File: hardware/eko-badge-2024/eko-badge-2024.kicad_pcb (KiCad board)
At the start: 2 copper layers, 45 x 95 mm, 1 part

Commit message: feat(Hw):Added_Lentes_project
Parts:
- removed the Ref** at (128.2, 66.4)
- added REF**: PinSocket_2x03_P2.54mm_Vertical, Connector_PinSocket_2.54mm:PinSocket_2x03_P2.54mm_Vertical, F.Cu at (190.4, 70.9)
- added Ref**: Val**, Eko2024:llama 1 flaca, F.Cu at (203.5, 80.0)
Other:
- board size 45 x 95 mm -> 47.5 x 99.9 mm

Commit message: feat(Hw):Added_First_Route
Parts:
- removed REF**: PinSocket_2x03_P2.54mm_Vertical, Connector_PinSocket_2.54mm:PinSocket_2x03_P2.54mm_Vertical
- added AE1: Antenna_Shield, Eko2024:SMA_EDGE, B.Cu at (221.3, 109.9)
- added C1: 10uF, Capacitor_SMD:C_0603_1608Metric, B.Cu at (221.5, 47.7)
- added C10: .1uF, Capacitor_SMD:C_0603_1608Metric, F.Cu at (194.1, 126.0)
- added C11: .1uF, Capacitor_SMD:C_0603_1608Metric, F.Cu at (205.4, 118.5)
- added C12: 0.1uF, Capacitor_SMD:C_0603_1608Metric, B.Cu at (204.2, 112.5)
- added C13: .22uF, Capacitor_SMD:C_0603_1608Metric, B.Cu at (202.1, 107.5)
- added C14: .1uF, Capacitor_SMD:C_0603_1608Metric, B.Cu at (211.2, 107.5)
- added C15: 1uF, Capacitor_SMD:C_0603_1608Metric, B.Cu at (207.2, 112.5)
- added C16: 0.1uF, Capacitor_SMD:C_0603_1608Metric, F.Cu at (207.7, 107.9)
- added C17: 0.1uF, Capacitor_SMD:C_0603_1608Metric, F.Cu at (194.6, 69.3)
- added C18: 0.1uF, Capacitor_SMD:C_0603_1608Metric, F.Cu at (216.1, 69.1)
- added C2: 1uF, Capacitor_SMD:C_0603_1608Metric, B.Cu at (189.6, 106.7)
- added C3: 10uF, Capacitor_SMD:C_0603_1608Metric, B.Cu at (219.3, 44.0)
- added C4: 10uF, Capacitor_SMD:C_0603_1608Metric, B.Cu at (186.8, 106.7)
- added C5: 10uF, Capacitor_SMD:C_0603_1608Metric, B.Cu at (186.7, 108.3)
- added C6: .1uF, Capacitor_SMD:C_0603_1608Metric, F.Cu at (201.9, 120.9)
- added C7: .1uF, Capacitor_SMD:C_0603_1608Metric, F.Cu at (202.6, 117.5)
- added C8: .1uF, Capacitor_SMD:C_0603_1608Metric, F.Cu at (204.6, 121.5)
- added C9: .1uF, Capacitor_SMD:C_0603_1608Metric, F.Cu at (210.7, 124.4)
- added D1: MBR120, Diode_SMD:D_SOD-123F, B.Cu at (221.4, 41.1)
- added D2: WS2812B, LED_SMD:LED_WS2812B-Mini_PLCC4_3.5x3.5mm, F.Cu at (203.6, 107.5)
- added D3: WS2812B, LED_SMD:LED_WS2812B-Mini_PLCC4_3.5x3.5mm, F.Cu at (194.1, 72.1)
- added D4: WS2812B, LED_SMD:LED_WS2812B-Mini_PLCC4_3.5x3.5mm, F.Cu at (217.2, 71.9)
- added F1: 0.75A, Fuse:Fuse_0805_2012Metric, B.Cu at (191.4, 46.8)
- added J1: UART, Connector_PinHeader_2.54mm:PinHeader_1x04_P2.54mm_Vertical, B.Cu at (184.2, 76.0)
- added J2: Battery, Eko2024:BH-AA-A1AJ020, B.Cu at (212.3, 77.6)
- added J3: Lentes, Connector_PinSocket_2.54mm:PinSocket_2x03_P2.54mm_Vertical, F.Cu at (185.0, 68.3)
- added J4: OLED, Eko2024:Display OLED 128 x32, F.Cu at (189.0, 95.6)
- added J7: Battery, Eko2024:BH-AA-A1AJ020, B.Cu at (194.1, 77.6)
- added LS1: 931-SPKM.20.8.A-ND, Connector_PinHeader_1.27mm:PinHeader_1x02_P1.27mm_Vertical, F.Cu at (213.5, 110.9)
- added P1: USB_C_Plug_USB2.0, Eko2024:C393939, B.Cu at (187.5, 43.3)
- added Q1: DMG3415U-7, Package_TO_SOT_SMD:SOT-23, B.Cu at (220.9, 38.0)
- added R1: 100K, Resistor_SMD:R_0603_1608Metric, B.Cu at (224.4, 44.0)
- added R2: 10K, Resistor_SMD:R_0603_1608Metric, B.Cu at (189.6, 108.2)
- added R3: 5k1, Resistor_SMD:R_0603_1608Metric, B.Cu at (191.2, 45.0)
- added R4: 5k1, Resistor_SMD:R_0603_1608Metric, B.Cu at (191.2, 43.5)
- added R5: 47K, Resistor_SMD:R_0603_1608Metric, B.Cu at (200.5, 107.5)
- added R6: 22K, Resistor_SMD:R_0603_1608Metric, B.Cu at (211.2, 110.5)
- added R7: 470, Resistor_SMD:R_0603_1608Metric, B.Cu at (198.0, 107.9)
- added R8: 3.3K, Resistor_SMD:R_0603_1608Metric, B.Cu at (195.7, 107.9)
- added SW1: ON, Eko2024:MSK12C02, B.Cu at (224.2, 79.0)
- added SW2: LEFT, Button_Switch_SMD:SW_SPST_TL3342, F.Cu at (196.9, 119.5)
- added SW3: UP, Button_Switch_SMD:SW_SPST_TL3342, F.Cu at (203.3, 113.7)
- added SW4: DOWN, Button_Switch_SMD:SW_SPST_TL3342, F.Cu at (203.3, 125.4)
- added SW5: RESET, Button_Switch_SMD:SW_SPST_TL3342, F.Cu at (216.5, 126.6)
- added SW6: BOOT, Button_Switch_SMD:SW_SPST_TL3342, F.Cu at (187.8, 126.8)
- added SW7: RIGTH, Button_Switch_SMD:SW_SPST_TL3342, F.Cu at (210.5, 119.5)
- added U1: ESP32-C6-WROOM-1-N4, bsides:XCVR_ESP32-C6-WROOM-1-N8, B.Cu at (189.6, 119.4)
- added U2: AP2112K-3.3, Package_TO_SOT_SMD:SOT-23-5, B.Cu at (221.8, 44.6)
- added U3: RFM95W-868S2, RF_Module:HOPERF_RFM9XW_SMD, B.Cu at (211.9, 121.5)
- added U4: TPA321, Package_SO:SOP-8_3.9x4.9mm_P1.27mm, B.Cu at (206.6, 108.5)
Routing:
- net /VOUT: track 0.00 -> 190.5 mm, vias 0 -> 4
- net /D+: track 0.00 -> 88.8 mm, vias 0 -> 2
- net /D-: track 0.00 -> 86.0 mm, vias 0 -> 2
- net /RX: track 0.00 -> 63.7 mm, vias 0 -> 2
- net /EN: track 0.00 -> 60.0 mm, vias 0 -> 1
- net /TX: track 0.00 -> 59.9 mm, vias 0 -> 2
- net Net-(D2-DOUT): track 0.00 -> 59.2 mm, vias 0 -> 2
- net Net-(D1-K): track 0.00 -> 54.5 mm, vias 0 -> 2
- net GND: track 0.00 -> 50.5 mm, vias 0 -> 7
- net /DIO2: track 0.00 -> 47.8 mm, vias 0 -> 2
- net VBUS: track 0.00 -> 47.4 mm
- net /DIO0: track 0.00 -> 42.2 mm, vias 0 -> 2
- net Net-(D3-DOUT): track 0.00 -> 37.5 mm
- net /DIO1: track 0.00 -> 37.4 mm, vias 0 -> 2
- net /RIGHT: track 0.00 -> 32.6 mm, vias 0 -> 1
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- added copper zone on B.Cu, net GND
- added copper zone on F.Cu, net GND

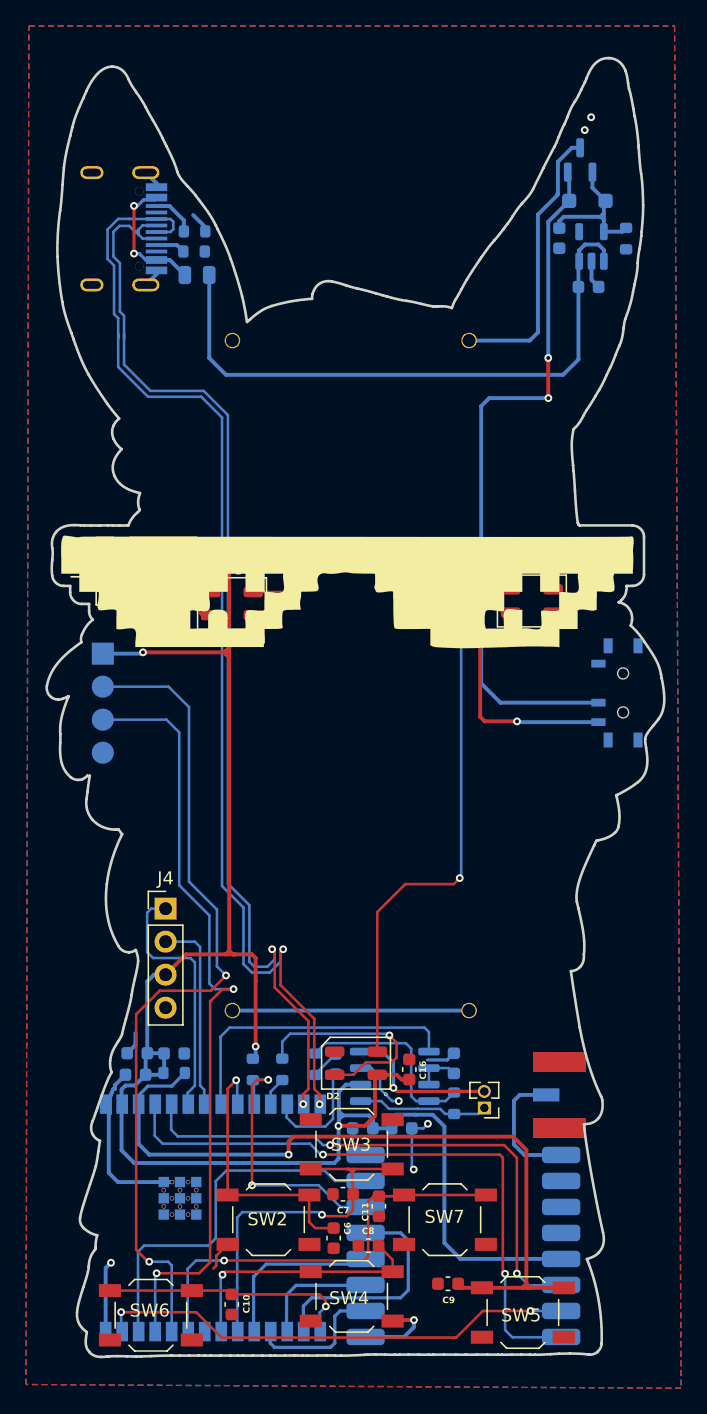
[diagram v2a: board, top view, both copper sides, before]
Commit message: feat(Hw):Update_Layer_Distribution
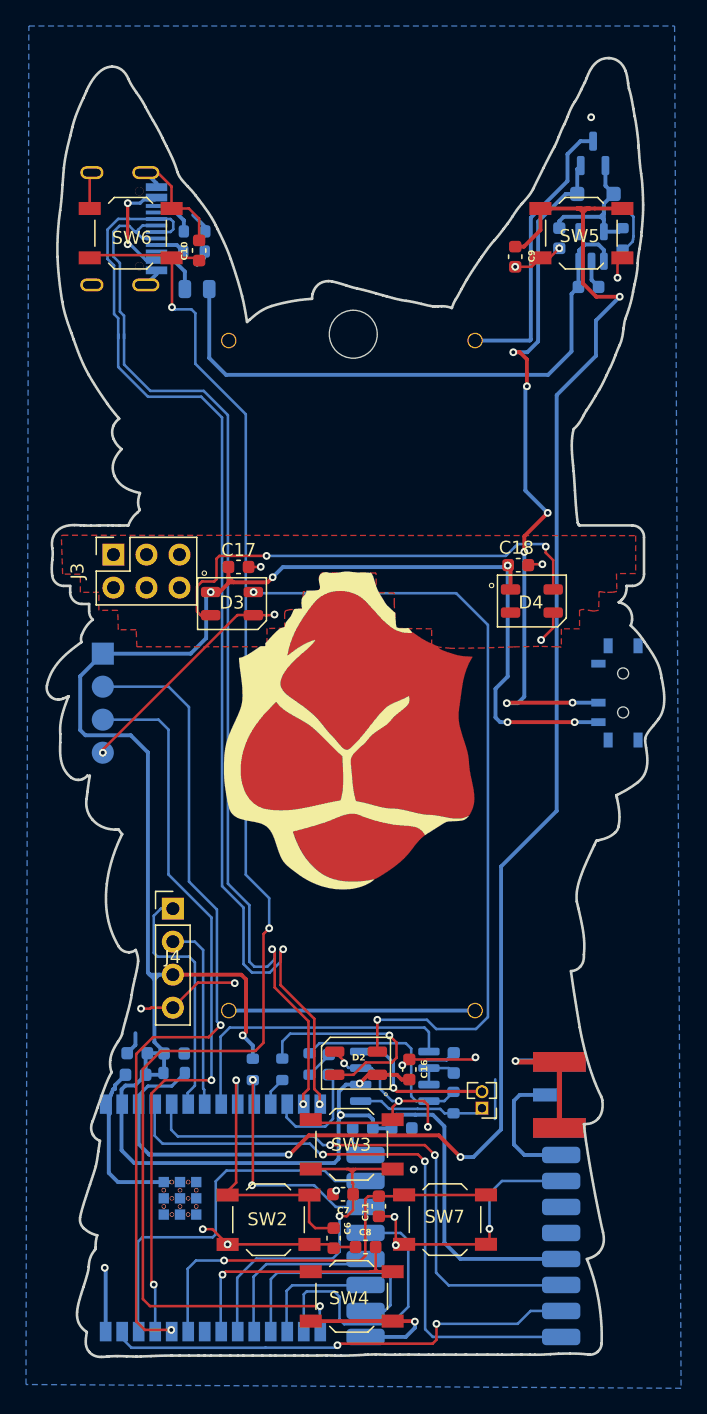
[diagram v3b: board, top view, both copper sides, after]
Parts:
- removed the Ref** at (203.5, 80.0)
- added Ref**: Val**, Eko2024:llama mask flaca, F.Cu at (203.7, 80.0)
- added Ref**: Val**, Eko2024:llama intermedia, F.Cu at (203.7, 80.1)
- moved SW6 83.3 mm to (186.3, 43.6), turned to 0 degrees
- moved SW5 83.2 mm to (221.0, 43.6)
- moved C10 81.1 mm to (191.6, 44.9), turned to -90 degrees
- moved C9 79.2 mm to (215.9, 45.4), turned to 90 degrees
- moved Q1 1.12 mm to (221.9, 37.5)
- moved F1 1.08 mm to (191.4, 47.9)
- moved D1 0.82 mm to (222.1, 40.6)
- moved J4 0.56 mm to (189.5, 95.6)
- moved C13 0.51 mm to (201.5, 107.6)
- moved J2 0.46 mm to (212.8, 77.6)
- moved R5 0.44 mm to (200.1, 107.5)
- moved J7 0.28 mm to (193.8, 77.6)
- moved R1 0.27 mm to (224.1, 44.0)
- moved C8 0.24 mm to (204.4, 121.6)
- moved LS1 0.18 mm to (213.3, 110.9)
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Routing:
- net GND: track 50.5 -> 170.4 mm, vias 7 -> 26
- net /BOOT: track 19.8 -> 116.8 mm, vias 1 -> 3
- net /EN: track 60.0 -> 127.3 mm, vias 1 -> 3
- net /VOUT: track 190.5 -> 182.3 mm, vias 4 -> 8
- net /CIPO: track 10.7 -> 17.8 mm
- net /CS: track 18.0 -> 22.3 mm
- net /TX: track 59.9 -> 57.2 mm
- net /RFM_RST: track 22.0 -> 19.8 mm
- net Net-(F1-Pad1): track 10.3 -> 12.2 mm
- net VBUS: track 47.4 -> 45.6 mm
- net Net-(D2-DOUT): track 59.2 -> 60.9 mm
- net Net-(D3-DOUT): track 37.5 -> 35.8 mm, vias 0 -> 2
- net /UP: track 28.6 -> 27.2 mm
- net /DOWN: track 20.1 -> 21.4 mm
- net /DIO1: track 37.4 -> 36.2 mm
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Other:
- outline, holes or cut-outs redrawn

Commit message: feat(Hw):Added_Shitty_Add-on
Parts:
- added J5: Add-On, Connector_PinSocket_2.54mm:PinSocket_2x03_P2.54mm_Vertical_SMD, F.Cu at (216.9, 132.0)
- added J6: Add-On, Connector_PinSocket_2.54mm:PinSocket_2x03_P2.54mm_Vertical_SMD, F.Cu at (188.0, 132.4)
- added kibuzzard-66BD383E: G***, kibuzzard-66BD383E, F.Cu at (203.1, 136.1)
- C12, C16, C17, C18: value 0.1uF -> .1uF
- U2: value AP2112K-3.3 -> XC6220B331MR-G
- moved J4 1.19 mm to (189.7, 96.7)
- moved D2 1.00 mm to (203.5, 108.5)
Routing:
- net /VOUT: track 182.3 -> 208.7 mm, vias 8 -> 10
- net /BOOT: track 116.8 -> 105.0 mm
- net GND: track 170.4 -> 181.0 mm, vias 26 -> 28
- net /SDA: track 19.2 -> 17.4 mm
- net /SCL: track 14.5 -> 13.2 mm
- net Net-(D2-DOUT): track 60.9 -> 62.0 mm
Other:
- board size 47.5 x 99.9 mm -> 47.5 x 108.1 mm

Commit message: feat(Hw): Change shitty add on
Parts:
- turned J5 to 135 degrees
- turned J6 to 45 degrees
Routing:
- net GND: track 181.0 -> 189.0 mm, vias 28 -> 27
- net /VOUT: track 208.7 -> 214.7 mm
- net /RX: track 64.3 -> 65.0 mm
- net /BOOT: track 105.0 -> 105.7 mm

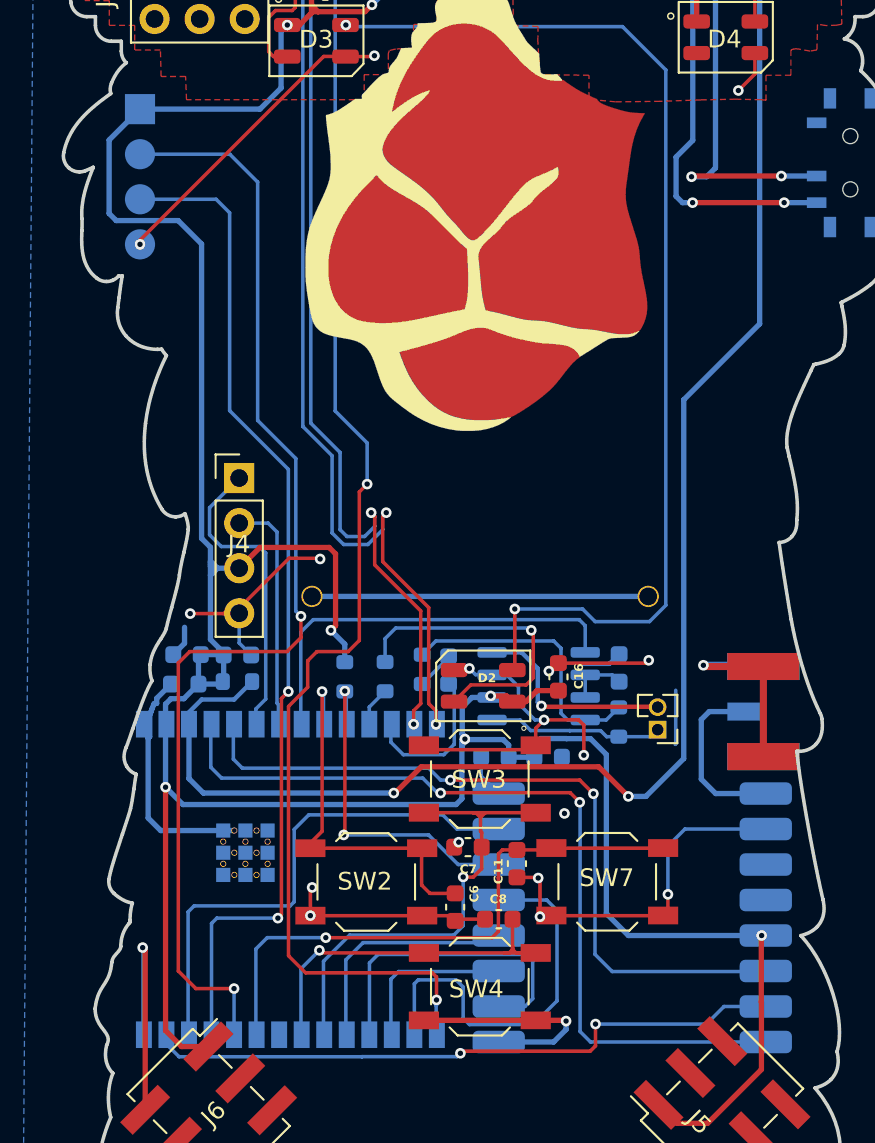
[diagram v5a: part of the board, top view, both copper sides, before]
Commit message: feat(Hw): Update route
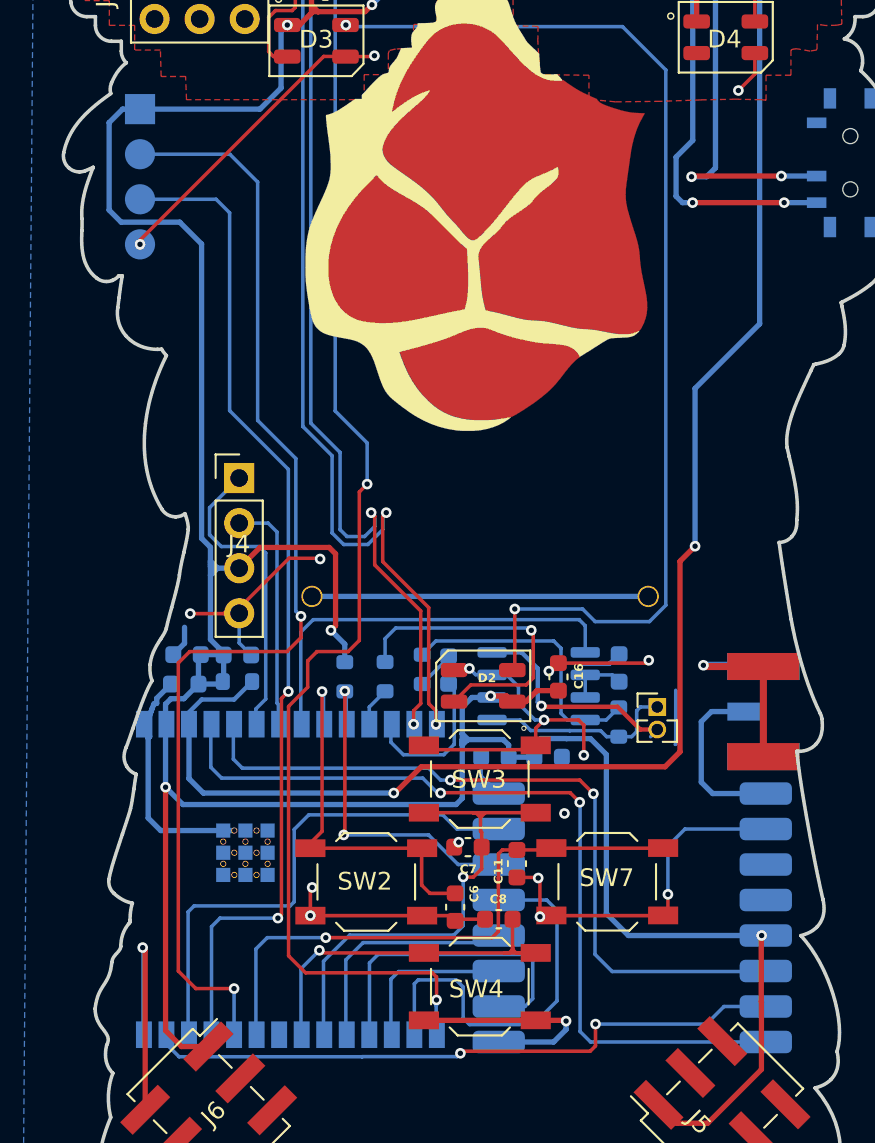
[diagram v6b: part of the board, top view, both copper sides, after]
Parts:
- moved LS1 1.28 mm to (213.3, 109.6), turned to 0 degrees
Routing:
- net /EN: track 127.3 -> 125.5 mm
- net Net-(U4-VO+): track 9.88 -> 11.1 mm
- net Net-(U4-VO-): track 11.7 -> 12.8 mm
- net /VOUT: track 214.7 -> 215.1 mm, vias 10 -> 9

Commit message: feat(Hw): Update PCB
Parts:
- removed the Ref** at (203.7, 80.1)
- added Ref**: Val**, Eko2024:eko-badge-2024-Edge_Cuts-Corte, F.Cu at (203.5, 84.2)
- moved kibuzzard-66BD383E 0.09 mm to (203.1, 136.2)

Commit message: feeat(Hw):Added_New_Cut
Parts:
- moved Ref** 0.29 mm to (203.7, 84.0)
